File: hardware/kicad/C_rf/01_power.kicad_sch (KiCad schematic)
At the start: 9 parts, among them U90 TPS62130

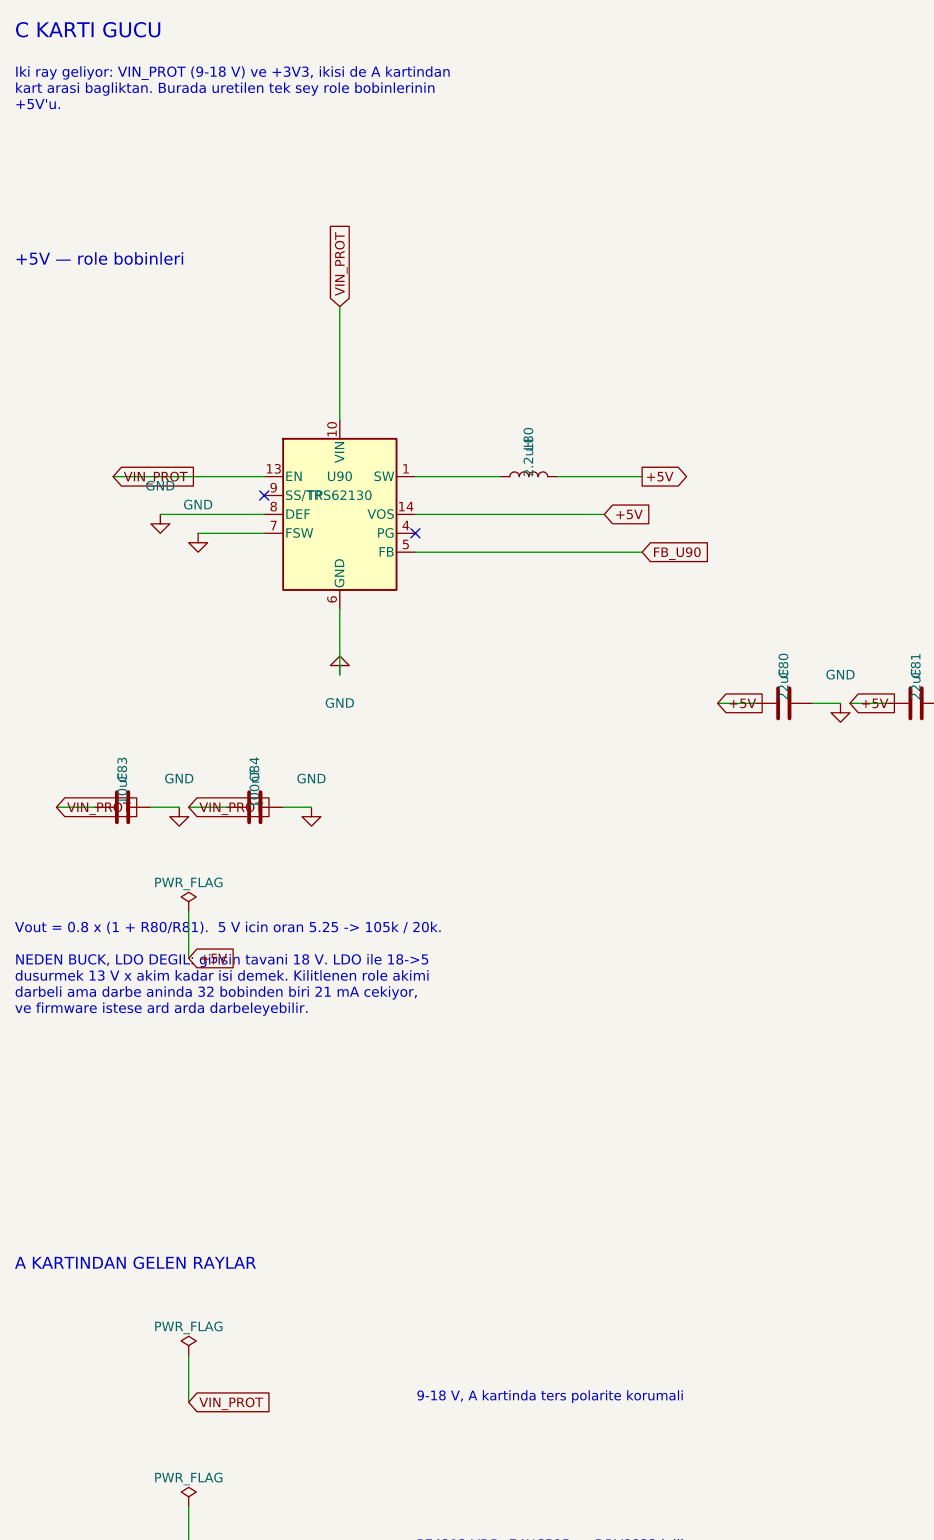
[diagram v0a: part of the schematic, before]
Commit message: Name the copyright holder and stamp it into the generated files
The repository had three licence files and no statement of who owns
the work. The only record of authorship was the git author field.

Copyleft depends on that statement. GPL and CERN-OHL-S work because
the holder grants permission on condition of reciprocity; with no
holder named there is nobody to require it from a downstream user.
Naming the author keeps the design open rather than closing it.

kicad/telif.py is the single source. The line reaches the schematics
through their title block and not through the generators, because
every schematic file is rewritten on each build and a header placed in
a generator would disappear at the first regeneration. All 23
schematics carry it. 109 source files have SPDX headers, split by the
project's own table: generators and the layout chain are hardware
under CERN-OHL-S-2.0, HDL and the audit tools are software under
GPL-3.0-only.

Board C's inductors also move to footprints that match parts that can
be bought. All of them sat on 0805 pads. Of the values this design
needs, 33 to 220 nH are 0603 parts, 470 and 820 nH are 0805, and
everything from 1000 nH upward is 1210, which is 3.2 by 2.5 mm and
does not fit an 0805 land. 32 inductors could not have been soldered.

A symbol-against-footprint check cannot find this. Those two agreed
with each other; what was wrong was the body size of the real part
behind the footprint.
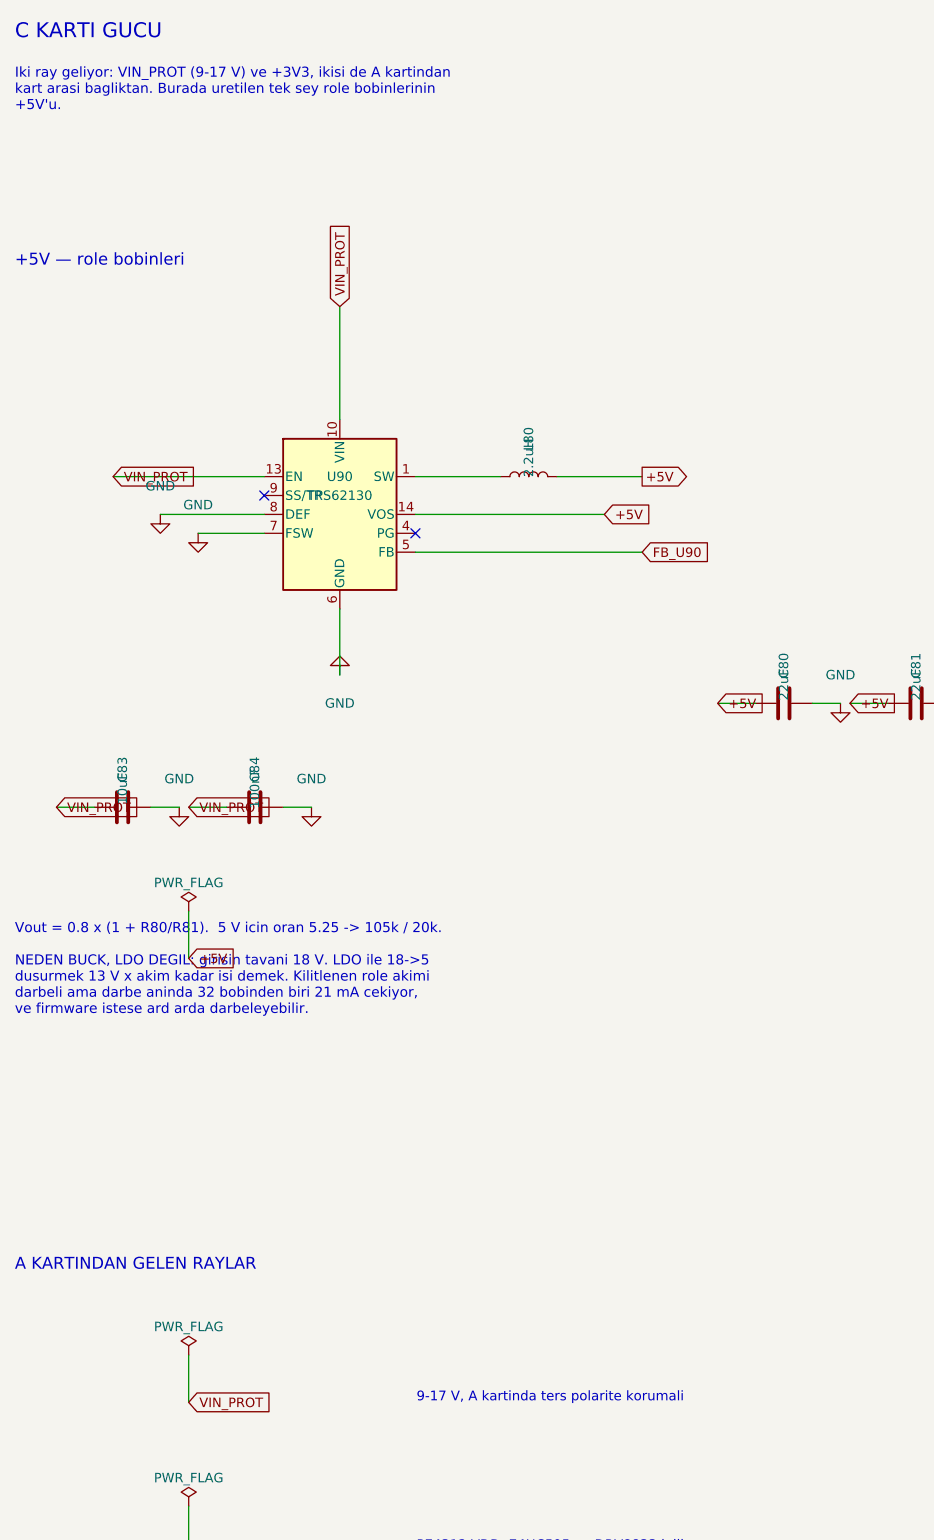
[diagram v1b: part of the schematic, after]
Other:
- note added: "9-17 V, A kartinda ters polarite korumali"
- note added: "Iki ray geliyor: VIN_PROT (9-17 V) ve +3V3, ikisi de A kartindan kart arasi bagliktan. Burada uretilen tek sey role bobinlerinin +5V'u."
- note removed: "9-18 V, A kartinda ters polarite korumali"
- note removed: "Iki ray geliyor: VIN_PROT (9-18 V) ve +3V3, ikisi de A kartindan kart arasi bagliktan. Burada uretilen tek sey role bobinlerinin +5V'u."
